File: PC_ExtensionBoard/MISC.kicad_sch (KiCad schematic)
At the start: 59 parts, among them J2 Conn_01x04_Pin, Q7 BSS138-7-F, Q8 BSS138-7-F, U37 9DBL0651CKILF, U38 74AUP2G132, U4 STM32G0B1RCT6, Y1 Oscillator_32.768kHz_ECS_2520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

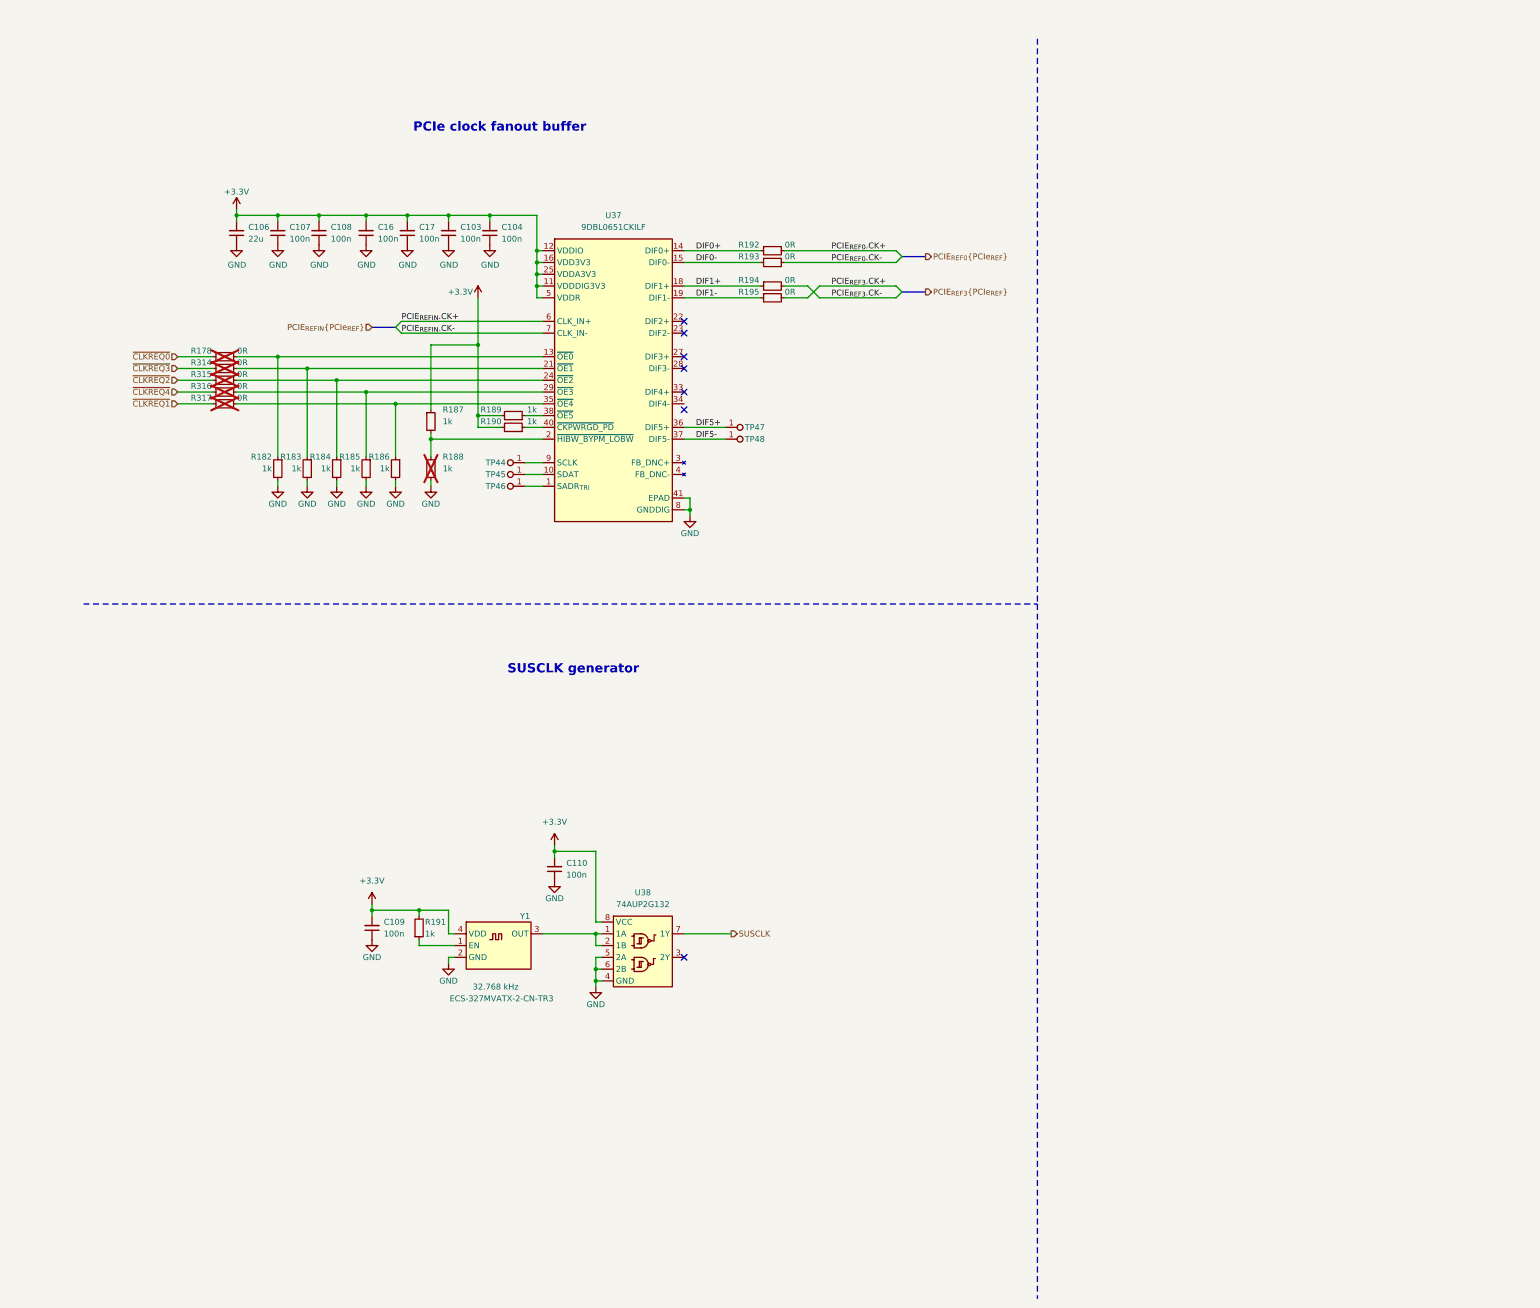
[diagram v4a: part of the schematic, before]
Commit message: update LCSC for HDMI
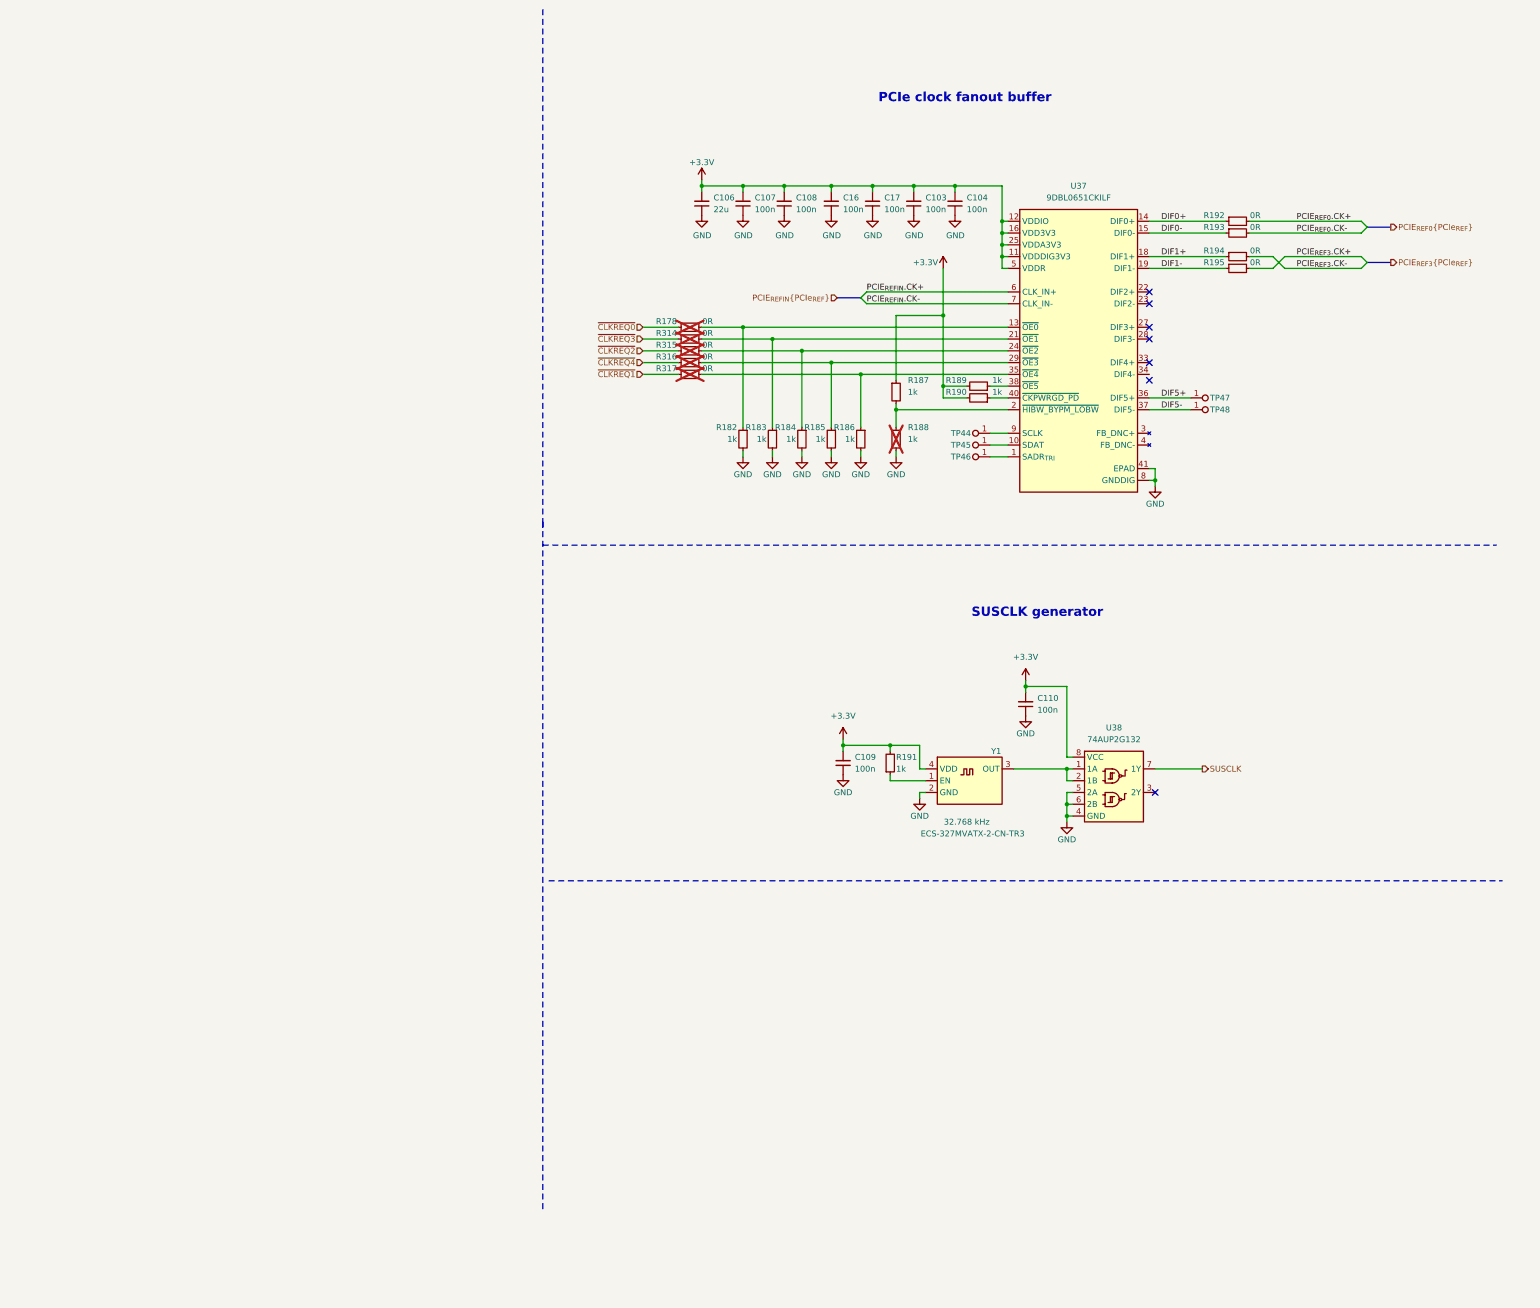
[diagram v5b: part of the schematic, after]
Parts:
- C103, C104, C107, C108, C109, C110, C112, C113, C114, C16, C17: LCSC (none) -> C85960
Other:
- moved on the sheet: C103, C104, C106, C107, C108, C109, C110, C16, C17, R178, R182, R183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

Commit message: update LCSC
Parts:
- added J3: Conn_01x16_MountingPin, symbol Connector_Generic_MountingPin:Conn_01x16_MountingPin
- C106: LCSC (none) -> C2762594
- D17, D18: LCSC (none) -> C2927824
- R140, R141, R142, R152, R153: LCSC (none) -> C202396
- R192: LCSC (none) -> C242160
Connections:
- net +5V: now also J3.10 (Pin_10), J3.11 (Pin_11), J3.12 (Pin_12), J3.9 (Pin_9)
- net GND: now also J3.1 (Pin_1), J3.13 (Pin_13), J3.14 (Pin_14), J3.15 (Pin_15), J3.16 (Pin_16), J3.4 (Pin_4), J3.5 (Pin_5), J3.8 (Pin_8)
- new net SATA0.RX+: J3.6 (Pin_6)
- new net SATA0.RX-: J3.7 (Pin_7)
- new net SATA0.TX+: J3.2 (Pin_2)
- new net SATA0.TX-: J3.3 (Pin_3)
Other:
- note added: "SATA CONN"
- moved on the sheet: D18, Q7, Q8, R152, R153

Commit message: schematic changes
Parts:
- J3: footprint (none) -> PC_Components_1:FPC-SMD_P0.50-16P_FGS-XJ-H2.0
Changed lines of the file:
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@@
 	(paper "A1")
 	(rectangle
-		(start 622.3 205.74)
+		(start 622.3 201.93)
 		(end 828.04 271.78)
 		(stroke
@@
 			)
 		)
-		(property "Footprint" ""
+		(property "Footprint" "PC_Components_1:FPC-SMD_P0.50-16P_FGS-XJ-H2.0"
 			(at 793.75 237.49 0)
 			(hide yes)

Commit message: update schematic
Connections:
- net MCU_USB_D+ renamed USB7.D+
- net MCU_USB_D- renamed USB7.D-
